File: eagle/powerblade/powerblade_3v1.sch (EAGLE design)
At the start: 56 parts, among them J21 AC_INTBFILM, U1 TPS62122, U5 MAX9910, U6 MAX9910, U7 OPA2369

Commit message: updated powerfilm
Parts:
- removed CS+, TP9: TP_LONG, skyspecs:TP_LONG
- removed CS+1, RS+1, RS-1, TP6, TP7, VS+1: TP_SMD, skyspecs:TP_SMD
- removed R13: 10, rcl:R-US_R0603
- removed U5: MAX9910, powerfilm:MAX9910
- added C2: (no value), rcl:C-EUC0603
- added R2: (no value), rcl:R-US_R0603
- added U2: MCP6V3, powerfilm:MCP6V3
- TP1: value TP_SMD -> TP_LONG; device skyspecs:TP_SMD -> skyspecs:TP_LONG; DIGIKEY 5129K-ND -> 5126K-ND
- TP5: value TP_SMD -> TP_LONG; device skyspecs:TP_SMD -> skyspecs:TP_LONG; DIGIKEY 5126K-ND -> (none)
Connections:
- removed net N$11: C10.1, C4.1, C9.1, CS+.P$1, CS+1.P$1, L1.1, R13.1, R7.2, U1.VOUT
- new net N$1: R2.1, R37.2, TP4.P$1, U7G$2.OUT
- net +3V3: now also C10.1, C4.1, C9.1, L1.1, R7.2, U1.VOUT, U2.VCC; no longer R13.2, U5.VCC, VS+1.P$1
- net GND: now also C2.2, U2.VSS; no longer RS-1.P$1, U5.VSS
- net I_SENSE: now also C2.1, R2.2, TP1.P$1; no longer R37.2, TP4.P$1, TP7.P$1, U7G$2.OUT
- net N$38: now also U2.IN+; no longer U5.IN+
- net N$4: now also TP5.P$1
- net N$61: now also U2.OUT; no longer TP5.P$1, U5.OUT
- net N$65: now also U2.IN-; no longer U5.IN-
- net N$67: no longer TP6.P$1, TP9.P$1
- net VCC: no longer RS+1.P$1
- net V_SENSE: no longer TP1.P$1
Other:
- note removed: "Current Sense"
- moved on the sheet: R37, R38, TP1, TP4

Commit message: updated schematic for powerblade 3v1
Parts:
- removed TP5: TP_LONG, skyspecs:TP_LONG
- added C14: 0.1uF, rcl:C-EUC0603
- added C15: 10uF, rcl:C-EUC0603
- added C16: 470nF, rcl:C-EUC0603
- added C34, C6: 8pF, rcl:C-EUC0603
- added C5: 33uF, rcl:C-EUC0603
- added J1: JTAG_14PIN_IDC, ibat:JTAG_14PIN_IDC
- added LED1, LED2: (no value), SparkFun-LED:LED0603
- added Q2, Q3: 2SK1829, powerfilm:2SK1829
- added R10, R23: 120, rcl:R-US_R0603
- added R11: 134k 1%, rcl:R-US_R0603
- added R12: 67k 1%, rcl:R-US_R0603
- added R19: 47k, rcl:R-US_R0603
- added R3: (no value), rcl:R-US_R1210
- added R33, R34: NP, rcl:R-US_R0603
- added TP10, TP11, TP12, TP13, TP14: TP_STD, skyspecs:TP_STD
- added U3: MSP430FR5738, powerfilm:MSP430FR5738
- added X3: 32.768kHz, general:CRYSTAL_0805
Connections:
- removed net N$4: C1.1, D1.A, D2.C, R8.2, TP5.P$1
- new net CNT0: U3.P1.0/VREF-
- new net CNT1: U3.P1.1/VREF+
- new net LTC_RX: R33.1, TP13.P$1, U3.P2.0/UCATX/MOSI
- new net LTC_SLEEP: U3.P2.2/UCBCLK
- new net LTC_TX: R34.1, TP12.P$1, U3.P2.1/TB0.0/UCARX/MISO
- new net METER_EN: U3.P1.7/TA1.0/UCBSCL/MISO
- new net N$23: C16.2, U3.VCORE
- new net N$3: C34.2, U3.XOUT, X3.P1
- new net N$49: LED1.A, R10.1
- new net N$54: LED1.C, Q2.D
- new net N$56: C6.2, U3.XIN, X3.P2
- new net N$58: LED2.A, R23.1
- new net N$59: LED2.C, Q3.D
- new net RST: J1.11, R19.1, U3.RST
- new net RXDATA: R34.2, TP11.P$1, U3.P1.6/TA0.0/UCBSDA/MOSI
- new net TCK: J1.7, Q2.G, U3.TCK
- new net TDI: J1.3, Q3.G, U3.TDI
- new net TDO: J1.1, U3.TDO
- new net TEST: J1.8, U3.TEST
- new net TMS: J1.5, U3.TMS
- new net TXMOD: R33.2, TP10.P$1, U3.P1.2/TA1.1/A2
- new net VCC_SENSE: R11.1, R12.2, U3.P1.3/TA1.2/A3
- new net ZC: C1.1, D1.A, D2.C, R3.2, R8.2
- net +3V3: now also C14.1, C15.1, J1.2, R10.2, R19.2, R23.2, U3.AVCC, U3.DVCC
- net GND: now also C14.2, C15.2, C16.1, C34.1, C5.2, C6.1, J1.9, Q2.S, Q3.S, R12.1, TP14.P$1, U3.AVSS, U3.DVSS
- net I_SENSE: now also U3.P1.5/TB0.2/UCACLK
- net VCC: now also C5.1, R11.2
- net VTEST: now also R3.1
- net V_SENSE: now also U3.P1.4/TB0.1/A4
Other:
- note added: "Co-locate C1 & R3 to save space"
- note added: "Ensure gap in both > 1.25mm"
- note removed: "Populate R4, R5, & R6 with 0ohm"
- note removed: "Remove R2 and R3"
- note removed: "Replace D2 with 0ohm"
- note removed: "To Make Full Wave:"

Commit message: finished new_final powerblade schematic
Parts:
- removed LED1: (no value), SparkFun-LED:LED0603
- removed Q2: 2SK1829, powerfilm:2SK1829
- removed R33, R34: NP, rcl:R-US_R0603
- removed TP10, TP11, TP12, TP13, TP14: TP_STD, skyspecs:TP_STD
- removed TP4: TP_LONG, skyspecs:TP_LONG
- added A1: FRACTUS-2.4GHZ-FR05-S1-N-0-102, chips:FRACTUS-2.4GHZ-FR05-S1-N-0-102
- added B1: BAL-NRF01D3, chips:BAL-NRF01D3
- added C11: 0.1uF, passives:CAPACITOR
- added C12, C20: 1nF, passives:CAPACITOR
- added C13: 4.7uF, passives:CAPACITOR
- added C17: 1uF, passives:CAPACITOR
- added C18, C19, C24, C25: 12pF, passives:CAPACITOR
- added C21: 47nF, passives:CAPACITOR
- added C22: 2.2nF, passives:CAPACITOR
- added C23: 0.8pF, passives:CAPACITOR
- added J4: TC2030-JLINK-NL, connector:TC2030-JLINK-NL
- added L2: 15nH, passives:INDUCTOR0402
- added L4: 10uH, passives:INDUCTOR0603
- added Q1: 2N7002, nav:2N7002
- added Q4: 2SK1829, powerfilm:2SK1829
- added R4: 12k, passives:RESISTOR
- added R5, R6: 220k, rcl:R-US_R0603
- added U4: NRF51822QF, chips:NRF51822QF
- added X1: 16MHz, crystals:TXC-8Y
- added X2: ABS05-32.768KHZ-9-T, crystals:ABS05-32.768KHZ-9-T
- C10: value 4.7uF -> 22uF; DIGIKEY 587-2786-1-ND -> (none)
- C7: device rcl:C-EUC0402 -> rcl:C-EUC0603; DIGIKEY 587-2786-1-ND -> (none)
- C8, C9: DIGIKEY 1276-1001-1-ND -> (none)
- R10: value 120 -> 220k; DIGIKEY P120GCT-ND -> (none)
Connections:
- removed net CNT0: U3.P1.0/VREF-
- removed net CNT1: U3.P1.1/VREF+
- removed net LTC_RX: R33.1, TP13.P$1, U3.P2.0/UCATX/MOSI
- removed net LTC_SLEEP: U3.P2.2/UCBCLK
- removed net LTC_TX: R34.1, TP12.P$1, U3.P2.1/TB0.0/UCARX/MISO
- removed net METER_EN: U3.P1.7/TA1.0/UCBSCL/MISO
- removed net N$49: LED1.A, R10.1
- removed net N$54: LED1.C, Q2.D
- removed net RXDATA: R34.2, TP11.P$1, U3.P1.6/TA0.0/UCBSDA/MOSI
- removed net TXMOD: R33.2, TP10.P$1, U3.P1.2/TA1.1/A2
- new net A0: C24.1, U4.P26/AIN0/XL2, X2.1
- new net A1: C25.1, U4.P27/AIN1/XL1, X2.2
- new net AVDD: C12.1, C17.1, L2.1, U4.AVDD
- new net BLE_ENABLE: Q1.G, R5.1, U3.P2.2/UCBCLK
- new net BLE_LPINT: U3.P1.6/TA0.0/UCBSDA/MOSI, U4.P30
- new net DCC: L4.2, U4.DCC
- new net FROMBLE_RX: U3.P2.1/TB0.0/UCARX/MISO, U4.P29
- new net GND2: B1.GND, C11.2, C12.2, C13.2, C17.2, C18.2, C19.2, C20.2, C21.2, C22.2, C23.2, C24.2, C25.2, J4.GND, Q1.D, R4.2, U4.GND
- new net GND3: C2.2, C27.2, C28.2, C38.2, Q4.D, R16.1, R18.1, R21.1, R38.1, R39.1, RI2.1, U2.VSS, U6.VSS, U7G$1.VSS
- new net METER_ENABLE: Q4.G, R6.1, U3.P1.7/TA1.0/UCBSCL/MISO
- new net N$14: L2.2, L4.1
- new net N$16: C18.1, U4.XC1, X1.1
- new net N$17: C19.1, U4.XC2, X1.2
- new net N$18: C20.1, U4.DEC1
- new net N$19: C21.1, U4.DEC2
- new net N$4: A1.ANTENNA, B1.SE, C23.1
- new net N$5: B1.ANT1, U4.ANT1
- new net N$6: B1.ANT2, U4.ANT2
- new net SWDCLK: J4.SWCLK, R4.1, U4.SWDCLK
- new net SWDIO/!RESET: J4.SWDIO, U4.SWDIO/!RESET
- new net TOBLE_TX: U3.P2.0/UCATX/MOSI, U4.P28
- new net VDD_PA: B1.VDD_PA, C22.1, U4.VDD_PA
- net +3V3: now also C11.1, C13.1, J4.VCC, U4.VDD; no longer R10.2
- net GND: now also Q1.S, Q4.S, R10.2, R5.2, R6.2; no longer C2.2, C27.2, C28.2, C38.2, Q2.S, R16.1, R18.1, R21.1, R38.1, R39.1, RI2.1, TP14.P$1, U2.VSS, U6.VSS, U7G$1.VSS
- net N$1: no longer TP4.P$1
- net TCK: no longer Q2.G
- net TDI: now also R10.1
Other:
- note added: "JTAG Connection"
- note added: "PIN1"
- note added: "PIN12"
- note added: "PIN36"
- moved on the sheet: LED2, Q3, R10, R11, R12, R23, VS+

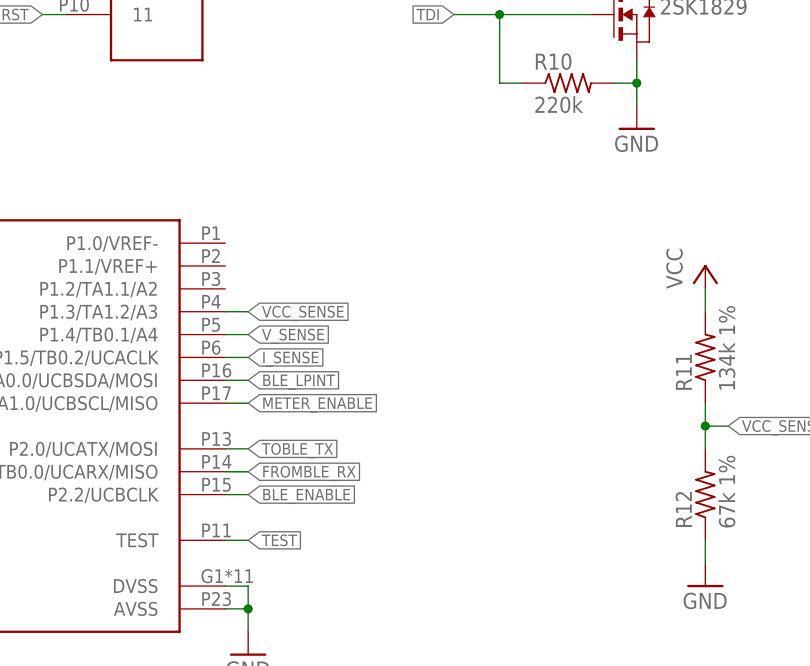
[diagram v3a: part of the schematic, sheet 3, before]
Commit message: added zc voltage divider to powerblade_3v1 schematic
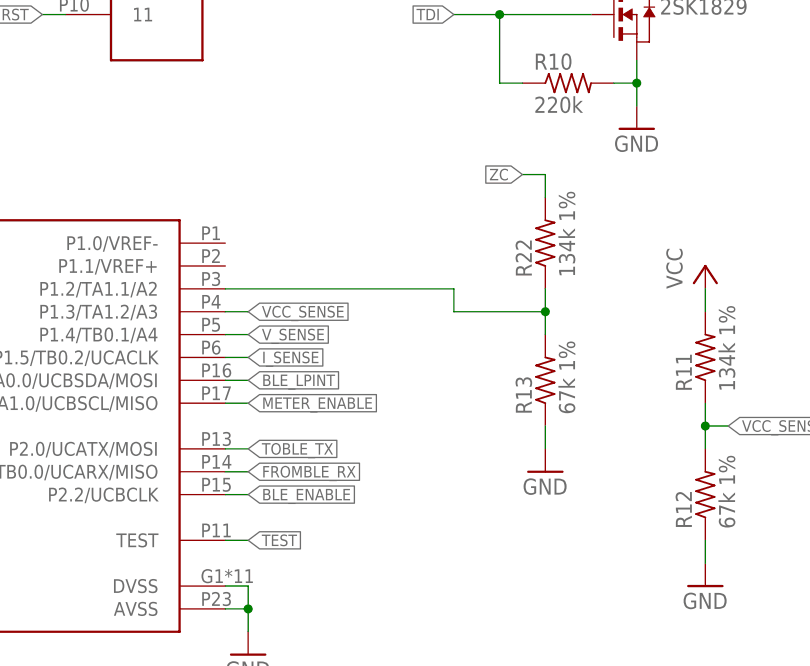
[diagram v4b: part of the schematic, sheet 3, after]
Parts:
- added R13: 67k 1%, rcl:R-US_R0603
- added R22: 134k 1%, rcl:R-US_R0603
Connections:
- new net N$8: R13.2, R22.1, U3.P1.2/TA1.1/A2
- net GND: now also R13.1
- net ZC: now also R22.2
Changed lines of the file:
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@@
 <grid distance="0.1" unitdist="inch" unit="inch" style="lines" multiple="1" display="no" altdistance="0.01" altunitdist="inch" altunit="inch"/>
 <layers>
-<layer number="1" name="Top" color="4" fill="1" visible="yes" active="no"/>
-<layer number="2" name="Route2" color="1" fill="3" visible="yes" active="no"/>
-<layer number="3" name="Route3" color="4" fill="3" visible="yes" active="no"/>
-<layer number="4" name="Route4" color="1" fill="4" visible="yes" active="no"/>
-<layer number="5" name="Route5" color="4" fill="4" visible="yes" active="no"/>
-<layer number="6" name="Route6" color="1" fill="8" visible="yes" active="no"/>
-<layer number="7" name="Route7" color="4" fill="8" visible="yes" active="no"/>
-<layer number="8" name="Route8" color="1" fill="2" visible="yes" active="no"/>
-<layer number="9" name="Route9" color="4" fill="2" visible="yes" active="no"/>
-<layer number="10" name="Route10" color="1" fill="7" visible="yes" active="no"/>
-<layer number="11" name="Route11" color="4" fill="7" visible="yes" active="no"/>
-<layer number="12" name="Route12" color="1" fill="5" visible="yes" active="no"/>
-<layer number="13" name="Route13" color="4" fill="5" visible="yes" active="no"/>
-<layer number="14" name="Route14" color="1" fill="6" visible="yes" active="no"/>
-<layer number="15" name="Route15" color="4" fill="6" visible="yes" active="no"/>
-<layer number="16" name="Bottom" color="1" fill="1" visible="yes" active="no"/>
-<layer number="17" name="Pads" color="2" fill="1" visible="yes" active="no"/>
-<layer number="18" name="Vias" color="2" fill="1" visible="yes" active="no"/>
-<layer number="19" name="Unrouted" color="6" fill="1" visible="yes" active="no"/>
-<layer number="20" name="Dimension" color="15" fill="1" visible="yes" active="no"/>
-<layer number="21" name="tPlace" color="7" fill="1" visible="yes" active="no"/>
-<layer number="22" name="bPlace" color="7" fill="1" visible="yes" active="no"/>
-<layer number="23" name="tOrigins" color="15" fill="1" visible="yes" active="no"/>
-<layer number="24" name="bOrigins" color="15" fill="1" visible="yes" active="no"/>
-<layer number="25" name="tNames" color="7" fill="1" visible="yes" active="no"/>
-<layer number="26" name="bNames" color="7" fill="1" visible="yes" active="no"/>
-<layer number="27" name="tValues" color="7" fill="1" visible="yes" active="no"/>
-<layer number="28" name="bValues" color="7" fill="1" visible="yes" active="no"/>
+<layer number="1" name="Top" color="4" fill="1" visible="no" active="no"/>
+<layer number="2" name="Route2" color="1" fill="3" visible="no" active="no"/>
+<layer number="3" name="Route3" color="4" fill="3" visible="no" active="no"/>
+<layer number="4" name="Route4" color="1" fill="4" visible="no" active="no"/>
+<layer number="5" name="Route5" color="4" fill="4" visible="no" active="no"/>
+<layer number="6" name="Route6" color="1" fill="8" visible="no" active="no"/>
+<layer number="7" name="Route7" color="4" fill="8" visible="no" active="no"/>
+<layer number="8" name="Route8" color="1" fill="2" visible="no" active="no"/>
+<layer number="9" name="Route9" color="4" fill="2" visible="no" active="no"/>
+<layer number="10" name="Route10" color="1" fill="7" visible="no" active="no"/>
+<layer number="11" name="Route11" color="4" fill="7" visible="no" active="no"/>
+<layer number="12" name="Route12" color="1" fill="5" visible="no" active="no"/>
+<layer number="13" name="Route13" color="4" fill="5" visible="no" active="no"/>
+<layer number="14" name="Route14" color="1" fill="6" visible="no" active="no"/>
+<layer number="15" name="Route15" color="4" fill="6" visible="no" active="no"/>
+<layer number="16" name="Bottom" color="1" fill="1" visible="no" active="no"/>
+<layer number="17" name="Pads" color="2" fill="1" visible="no" active="no"/>
+<layer number="18" name="Vias" color="2" fill="1" visible="no" active="no"/>
+<layer number="19" name="Unrouted" color="6" fill="1" visible="no" active="no"/>
+<layer number="20" name="Dimension" color="15" fill="1" visible="no" active="no"/>
+<layer number="21" name="tPlace" color="7" fill="1" visible="no" active="no"/>
+<layer number="22" name="bPlace" color="7" fill="1" visible="no" active="no"/>
+<layer number="23" name="tOrigins" color="15" fill="1" visible="no" active="no"/>
+<layer number="24" name="bOrigins" color="15" fill="1" visible="no" active="no"/>
+<layer number="25" name="tNames" color="7" fill="1" visible="no" active="no"/>
+<layer number="26" name="bNames" color="7" fill="1" visible="no" active="no"/>
+<layer number="27" name="tValues" color="7" fill="1" visible="no" active="no"/>
+<layer number="28" name="bValues" color="7" fill="1" visible="no" active="no"/>
 <layer number="29" name="tStop" color="7" fill="3" visible="no" active="no"/>
 <layer number="30" name="bStop" color="7" fill="6" visible="no" active="no"/>
@@
 <layer number="35" name="tGlue" color="7" fill="4" visible="no" active="no"/>
 <layer number="36" name="bGlue" color="7" fill="5" visible="no" active="no"/>
-<layer number="37" name="tTest" color="7" fill="1" visible="yes" active="no"/>
-<layer number="38" name="bTest" color="7" fill="1" visible="yes" active="no"/>
+<layer number="37" name="tTest" color="7" fill="1" visible="no" active="no"/>
+<layer number="38" name="bTest" color="7" fill="1" visible="no" active="no"/>
 <layer number="39" name="tKeepout" color="4" fill="11" visible="no" active="no"/>
 <layer number="40" name="bKeepout" color="1" fill="11" visible="no" active="no"/>
@@
 <layer number="44" name="Drills" color="7" fill="1" visible="no" active="no"/>
 <layer number="45" name="Holes" color="7" fill="1" visible="no" active="no"/>
-<layer number="46" name="Milling" color="3" fill="1" visible="yes" active="no"/>
-<layer number="47" name="Measures" color="7" fill="1" visible="yes" active="no"/>
-<layer number="48" name="Document" color="7" fill="1" visible="yes" active="no"/>
-<layer number="49" name="Reference" color="7" fill="1" visible="yes" active="no"/>
-<layer number="50" name="dxf" color="7" fill="1" visible="yes" active="no"/>
-<layer number="51" name="tDocu" color="7" fill="1" visible="yes" active="no"/>
-<layer number="52" name="bDocu" color="7" fill="1" visible="yes" active="no"/>
-<layer number="53" name="tGND_GNDA" color="7" fill="9" visible="yes" active="no"/>
-<layer number="54" name="bGND_GNDA" color="1" fill="9" visible="yes" active="no"/>
-<layer number="56" name="wert" color="7" fill="1" visible="yes" active="no"/>
-<layer number="57" name="tCAD" color="7" fill="1" visible="yes" active="no"/>
+<layer number="46" name="Milling" color="3" fill="1" visible="no" active="no"/>
+<layer number="47" name="Measures" color="7" fill="1" visible="no" active="no"/>
+<layer number="48" name="Document" color="7" fill="1" visible="no" active="no"/>
+<layer number="49" name="Reference" color="7" fill="1" visible="no" active="no"/>
+<layer number="50" name="dxf" color="7" fill="1" visible="no" active="no"/>
+<layer number="51" name="tDocu" color="7" fill="1" visible="no" active="no"/>
+<layer number="52" name="bDocu" color="7" fill="1" visible="no" active="no"/>
+<layer number="53" name="tGND_GNDA" color="7" fill="9" visible="no" active="no"/>
+<layer number="54" name="bGND_GNDA" color="1" fill="9" visible="no" active="no"/>
+<layer number="56" name="wert" color="7" fill="1" visible="no" active="no"/>
+<layer number="57" name="tCAD" color="7" fill="1" visible="no" active="no"/>
 <layer number="91" name="Nets" color="2" fill="1" visible="yes" active="yes"/>
 <layer number="92" name="Busses" color="1" fill="1" visible="yes" active="yes"/>
@@
 <part name="GND2" library="supply1" deviceset="GND" device=""/>
 <part name="R10" library="rcl" deviceset="R-US_" device="R0603" value="220k"/>
+<part name="R13" library="rcl" deviceset="R-US_" device="R0603" value="67k 1%">
+<attribute name="DIGIKEY" value="P66.5KHCT-ND"/>
+</part>
+<part name="R22" library="rcl" deviceset="R-US_" device="R0603" value="134k 1%">
+<attribute name="DIGIKEY" value="P133KHCT-ND"/>
+</part>
+<part name="GND8" library="supply1" deviceset="GND" device=""/>
 </parts>
 <sheets>
@@
 <instance part="GND27" gate="1" x="71.12" y="30.48"/>
 <instance part="R10" gate="G$1" x="63.5" y="35.56"/>
+<instance part="R13" gate="G$1" x="60.96" y="2.54" rot="R90">
+<attribute name="DIGIKEY" x="60.96" y="2.54" size="1.27" layer="96" rot="R90" display="off"/>
+</instance>
+<instance part="R22" gate="G$1" x="60.96" y="17.78" rot="R90">
+<attribute name="DIGIKEY" x="60.96" y="17.78" size="1.27" layer="96" rot="R90" display="off"/>
+</instance>
+<instance part="GND8" gate="1" x="60.96" y="-7.62"/>
 </instances>
 <busses>
@@
 <wire x1="68.58" y1="35.56" x2="71.12" y2="35.56" width="0.1524" layer="91"/>
 <junction x="71.12" y="35.56"/>
+</segment>
+<segment>
+<pinref part="R13" gate="G$1" pin="1"/>
+<pinref part="GND8" gate="1" pin="GND"/>
+<wire x1="60.96" y1="-2.54" x2="60.96" y2="-5.08" width="0.1524" layer="91"/>
 </segment>
 </net>
@@
 </segment>
 </net>
+<net name="ZC" class="0">
+<segment>
+<pinref part="R22" gate="G$1" pin="2"/>
+<wire x1="58.42" y1="25.4" x2="60.96" y2="25.4" width="0.1524" layer="91"/>
+<wire x1="60.96" y1="25.4" x2="60.96" y2="22.86" width="0.1524" layer="91"/>
+<label x="58.42" y="25.4" size="1.27" layer="95" rot="R180" xref="yes"/>
+</segment>
+</net>
+<net name="N$8" class="0">
+<segment>
+<pinref part="U3" gate="G$1" pin="P1.2/TA1.1/A2"/>
+<wire x1="25.4" y1="12.7" x2="50.8" y2="12.7" width="0.1524" layer="91"/>
+<wire x1="50.8" y1="12.7" x2="50.8" y2="10.16" width="0.1524" layer="91"/>
+<pinref part="R22" gate="G$1" pin="1"/>
+<wire x1="50.8" y1="10.16" x2="60.96" y2="10.16" width="0.1524" layer="91"/>
+<wire x1="60.96" y1="10.16" x2="60.96" y2="12.7" width="0.1524" layer="91"/>
+<pinref part="R13" gate="G$1" pin="2"/>
+<wire x1="60.96" y1="10.16" x2="60.96" y2="7.62" width="0.1524" layer="91"/>
+<junction x="60.96" y="10.16"/>
+</segment>
+</net>
